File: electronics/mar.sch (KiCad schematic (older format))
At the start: 13 parts, among them U13 74LS157, U14 74LS157, U15 74LS08, U16 74LS245, U17 74LS157, U18 74LS157, U19 74LS245

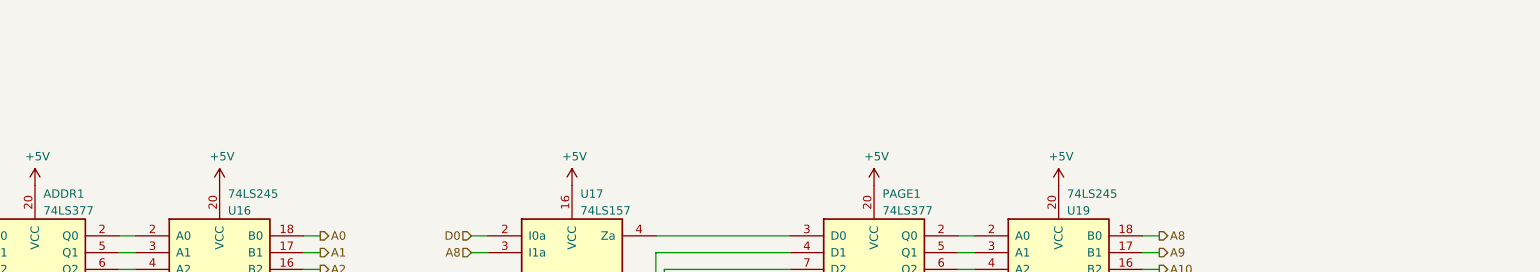
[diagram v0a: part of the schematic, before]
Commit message: Move electronics stuff into a subfolder
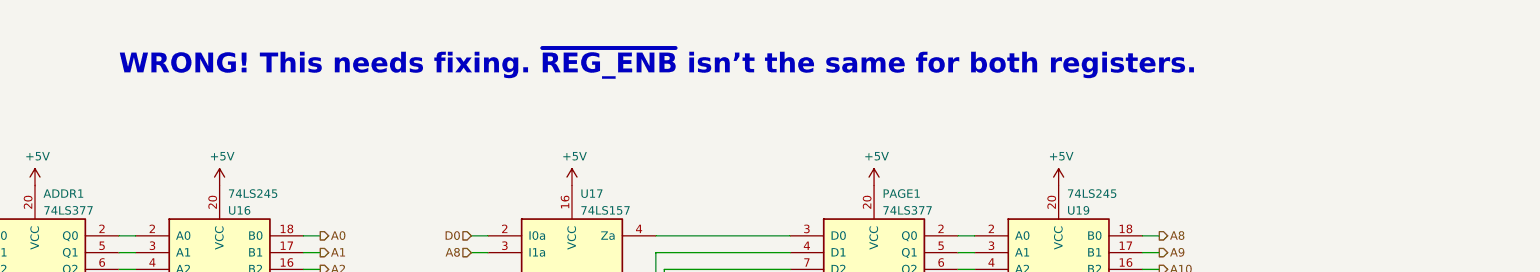
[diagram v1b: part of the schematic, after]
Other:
- note added: "WRONG! This needs fixing. ~REG_ENB~ isn’t the same for both registers."
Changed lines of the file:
@@
 Wire Wire Line
 	4000 4500 4000 4400
+Text Notes 4150 1100 0    118  ~ 24
+WRONG! This needs fixing. ~REG_ENB~ isn’t the same for both registers.
 $EndSCHEMATC

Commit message: Some initial electronics design
Not everything done yet, just committing to show progress and to get the changes out of the way.
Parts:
- removed ADDR1, PAGE1: 74LS377, Package_DIP:DIP-20_W7.62mm, symbol 74xx:74LS377
- removed C6, C7, C8, C9: 0.1µF, Capacitor_THT:CP_Radial_D4.0mm_P1.50mm, symbol Device:C
- removed U13, U14, U17, U18: 74LS157, Package_DIP:DIP-16_W7.62mm, symbol 74xx:74LS157
- removed U15: 74LS08, Package_DIP:DIP-14_W7.62mm, symbol 74xx:74LS08
- removed U16, U19: 74LS245, Package_DIP:DIP-20_W7.62mm, symbol 74xx:74LS245
- added U1: 74LS08, symbol 74xx:74LS08
- added U2: 74LS32, symbol 74xx:74LS32
- added U3, U4: 74LS273, symbol 74xx:74LS273
- added U5, U6: 74LS245, symbol 74xx:74LS245
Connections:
- net +5V: now also U1.14 (VCC), U2.14 (VCC), U3.20 (VCC), U4.20 (VCC), U5.1 (A->B), U5.20 (VCC), U6.1 (A->B), U6.20 (VCC)
- net A0: now also U5.18 (B0)
- net A1: now also U5.17 (B1)
- net A10: now also U6.16 (B2)
- net A11: now also U6.15 (B3)
- net A12: now also U6.14 (B4)
- net A13: now also U6.13 (B5)
- net A14: now also U6.12 (B6)
- net A15: now also U6.11 (B7)
- net A2: now also U5.16 (B2)
- net A3: now also U5.15 (B3)
- net A4: now also U5.14 (B4)
- net A5: now also U5.13 (B5)
- net A6: now also U5.12 (B6)
- net A7: now also U5.11 (B7)
- net A8: now also U6.18 (B0)
- net A9: now also U6.17 (B1)
- net GND: now also U1.7 (GND), U2.7 (GND), U3.10 (GND), U4.10 (GND), U5.10 (GND), U6.10 (GND)
- net ~CLK: now also U1.2, U1.5
- new net: U1.3, U3.11 (Cp)
- new net: U3.12 (Q4), U5.6 (A4)
- new net: U3.15 (Q5), U5.7 (A5)
- new net: U3.16 (Q6), U5.8 (A6)
- new net: U3.19 (Q7), U5.9 (A7)
- new net: U3.2 (Q0), U5.2 (A0)
- new net: U3.5 (Q1), U5.3 (A1)
- new net: U3.6 (Q2), U5.4 (A2)
- new net: U3.9 (Q3), U5.5 (A3)
- new net: U1.1, U2.3
- new net: U1.6, U4.11 (Cp)
- new net: U4.12 (Q4), U6.6 (A4)
- new net: U4.15 (Q5), U6.7 (A5)
- new net: U4.16 (Q6), U6.8 (A6)
- new net: U4.19 (Q7), U6.9 (A7)
- new net: U4.2 (Q0), U6.2 (A0)
- new net: U4.5 (Q1), U6.3 (A1)
- new net: U4.6 (Q2), U6.4 (A2)
- new net: U4.9 (Q3), U6.5 (A3)
- new net: U1.4, U2.6
- new net ADDR MUX/O0: U3.3 (D0)
- new net ADDR MUX/O1: U3.4 (D1)
- new net ADDR MUX/O2: U3.7 (D2)
- new net ADDR MUX/O3: U3.8 (D3)
- new net ADDR MUX/O4: U3.13 (D4)
- new net ADDR MUX/O5: U3.14 (D5)
- new net ADDR MUX/O6: U3.17 (D6)
- new net ADDR MUX/O7: U3.18 (D7)
- new net ADDR_IN: U2.1
- new net FROM_ADRB: U2.2, U2.5
- new net PAGE MUX/O0: U4.3 (D0)
- new net PAGE MUX/O1: U4.4 (D1)
- new net PAGE MUX/O2: U4.7 (D2)
- new net PAGE MUX/O3: U4.8 (D3)
- new net PAGE MUX/O4: U4.13 (D4)
- new net PAGE MUX/O5: U4.14 (D5)
- new net PAGE MUX/O6: U4.17 (D6)
- new net PAGE MUX/O7: U4.18 (D7)
- new net PAGE_IN: U2.4
- new net ~RESET: U3.1 (~Mr), U4.1 (~Mr)
- new net ~TO_ADRB: U5.19 (CE), U6.19 (CE)
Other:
- note removed: "WRONG! This needs fixing. ~REG_ENB~ isn’t the same for both registers."
